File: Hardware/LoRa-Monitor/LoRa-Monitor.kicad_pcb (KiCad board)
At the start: 4 copper layers, 102.6 x 148 mm, 246 parts, among them J1 USB_C_Receptacle_USB2.0_16P, J10 AudioJack3, J11 Screw_Terminal_01x02, J12 Screw_Terminal_01x02, J13 Conn_01x02_Pin, J14 Conn_01x02_Pin, J15 Screw_Terminal_01x03, J2 Micro_SD_Card, J3 Conn_02x03_Odd_Even, J4 Conn_Coaxial, J6 Screw_Terminal_01x02, J7 AudioJack3, J8 AudioJack3, J9 Screw_Terminal_01x04, Q1 MMBT5551L, Q2 MMBT5551L, Q3 MMBT5551L, Q4 MMBT5551L, Q5 MMBT5551L, Q6 MMBT5551L, U1 IRM-05-5, U10 ESP32-S3-WROOM-1, U11 TPS63021DSJR, U12 NXE1S0303MC, U13 NXE1S0303MC, U14 ATM90E32AS-AU-R, U15 E22-900M30S, U16 ADuM1401xRW, U17 ADuM1401xRW, U18 ADuM1401xRW, U2 ACPL-M61L, U3 ACPL-M61L, U4 ACPL-M61L, U5 ACPL-M61L, U6 ACPL-M61L, U7 ACPL-M61L, U8 MAX3485, U9 BQ24072RGT, Y1 16.384MHz

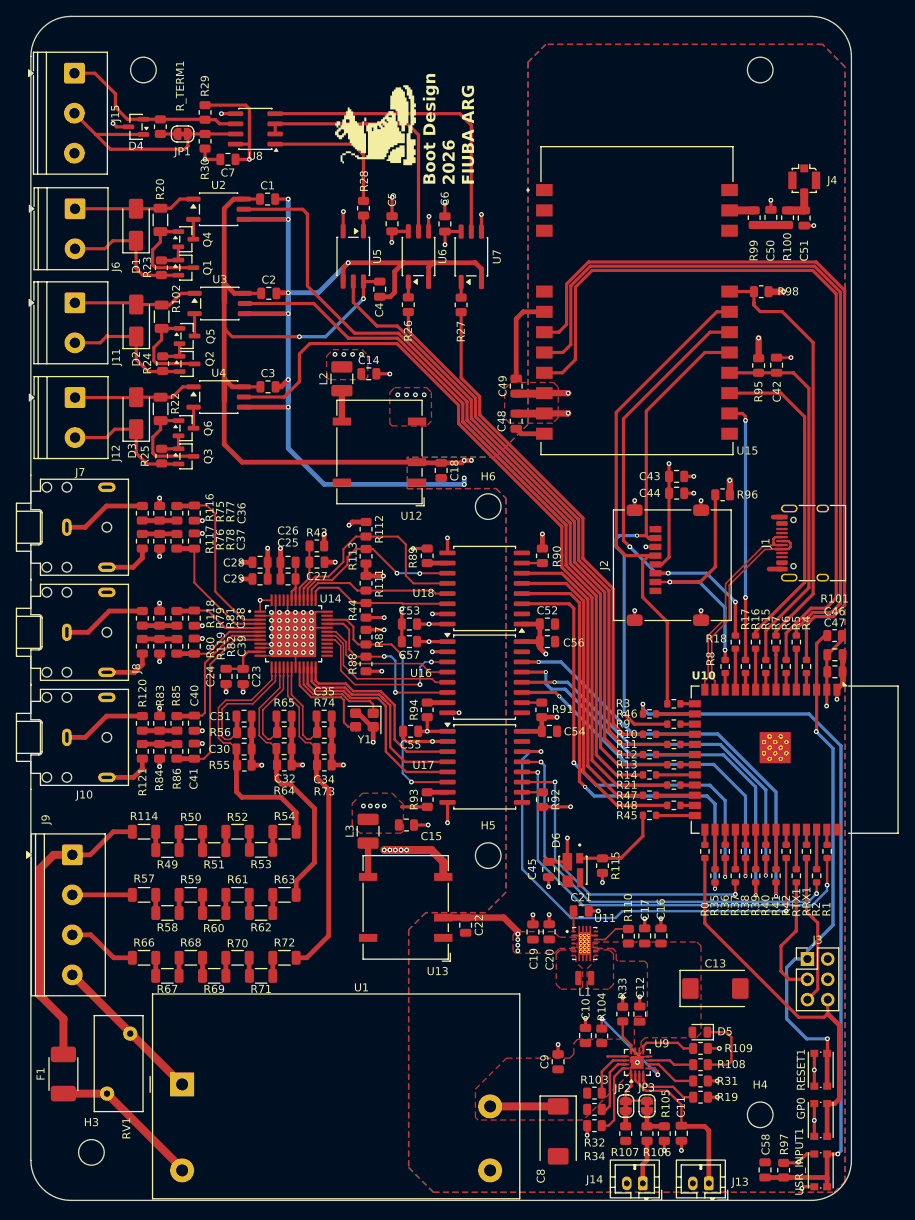
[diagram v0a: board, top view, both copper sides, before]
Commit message: Changed the RS485-TTL translator and its relevent componentes (Power source and optocuplers) for a simpler and easier solution using the ADM2582.
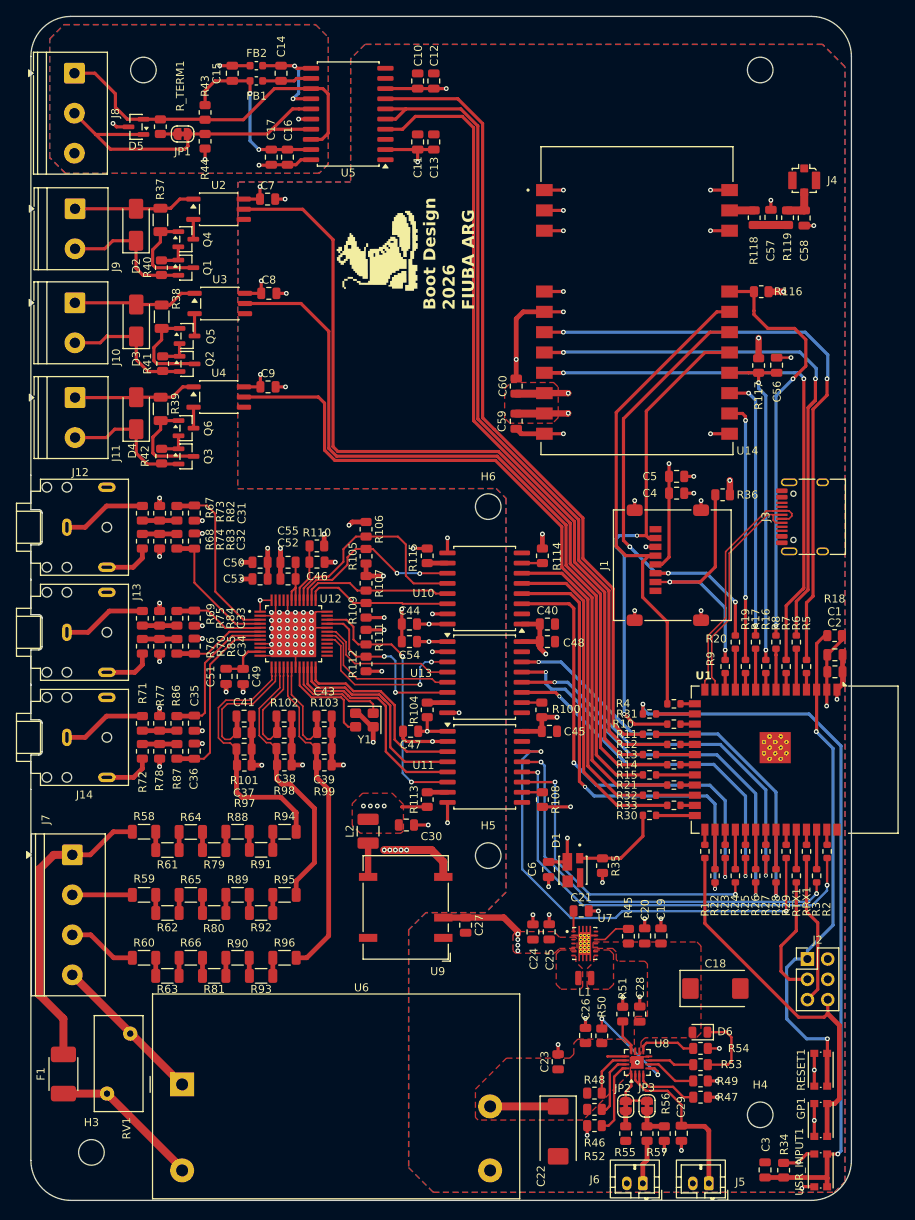
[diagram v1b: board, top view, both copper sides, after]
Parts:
- removed the C14 at (73.7, 66.7)
- removed the C18 at (82.7, 78.8)
- removed the C4 at (75.0, 56.1)
- removed the C6 at (83.2, 47.9)
- removed the C7 at (56.1, 39.9)
- removed the L2 at (70.3, 67.3)
- removed the R26 at (78.6, 58.0)
- removed the R27 at (85.2, 58.1)
- removed the R28 at (73.0, 46.0)
- removed the U12 at (75.0, 75.2)
- removed the U6 at (79.9, 52.0)
- removed the U7 at (86.5, 52.0)
- removed the U8 at (59.5, 36.1)
- added C10: 100nF, Capacitor_SMD:C_0805_2012Metric, F.Cu at (79.8, 30.1)
- added C11: 100nF, Capacitor_SMD:C_0805_2012Metric, F.Cu at (79.8, 37.7)
- added C12: 10uF, Capacitor_SMD:C_0805_2012Metric, F.Cu at (81.8, 30.1)
- added C13: 10nF, Capacitor_SMD:C_0805_2012Metric, F.Cu at (81.8, 37.7)
- added C15: 10uF, Capacitor_SMD:C_0805_2012Metric, F.Cu at (56.6, 29.1)
- added C16: 100nF, Capacitor_SMD:C_0805_2012Metric, F.Cu at (63.5, 39.6)
- added C17: 10nF, Capacitor_SMD:C_0805_2012Metric, F.Cu at (61.5, 39.6)
- added FB1: FerriteBead, Inductor_SMD:L_0603_1608Metric, F.Cu at (59.6, 30.1)
- added FB2: FerriteBead, Inductor_SMD:L_0603_1608Metric, F.Cu at (59.6, 28.2)
- C14: renamed from C5; value 100nF 50V X7R -> 100nF
- U5: value ACPL-M61L -> ADM2582E; footprint DeviceComponents:SO-5_4.39x3.84mm_P1.27mm -> Package_SO:SOIC-20W_7.5x12.8mm_P1.27mm
- moved C14 23.4 mm to (62.7, 29.1)
- moved U5 17.8 mm to (71.1, 34.2), turned to 180 degrees
- moved G*** 15.7 mm to (74.7, 51.3)
- moved J3 3.28 mm to (129.3, 84.5)
- renumbered C46 to C1, C13 to C18, C16 to C19, C47 to C2, C17 to C20, C8 to C22, C9 to C23, C19 to C24, C20 to C25, C10 to C26, C22 to C27, C12 to C28, C11 to C29, C58 to C3, C15 to C30, C36 to C31, C37 to C32, C38 to C33, C39 to C34, C40 to C35, C41 to C36, C30 to C37, C32 to C38, C34 to C39, C44 to C4, C52 to C40, C31 to C41, C33 to C42, C35 to C43, C53 to C44, C54 to C45, C27 to C46, C55 to C47, C56 to C48, C23 to C49, C43 to C5, C28 to C50, C24 to C51, C25 to C52, C29 to C53, C57 to C54, C26 to C55, C42 to C56, C50 to C57, C51 to C58, C48 to C59, C45 to C6, C49 to C60, C1 to C7, C2 to C8, C3 to C9, D6 to D1, D1 to D2, D2 to D3, D3 to D4, D4 to D5, D5 to D6, GP0 to GP1, J2 to J1, J11 to J10, J12 to J11, J7 to J12, J8 to J13, J10 to J14, J3 to J2, J1 to J3, J13 to J5, J14 to J6, J9 to J7, J15 to J8, J6 to J9, L3 to L2, R0 to R1, R9 to R10, R91 to R100, R56 to R101, R65 to R102, R74 to R103, R94 to R104, R113 to R105, R112 to R106, R111 to R107, R92 to R108, R44 to R109, R10 to R11, R43 to R110, R87 to R111, R88 to R112, R93 to R113, R90 to R114, R89 to R115, R98 to R116, R95 to R117, R99 to R118, R100 to R119, R11 to R12, R12 to R13, R13 to R14, R14 to R15, R15 to R16, R16 to R17, R101 to R18, R17 to R19, R1 to R2, R18 to R20, R35 to R22, R36 to R23, R37 to R24, R38 to R25, R39 to R26, R40 to R27, R41 to R28, R42 to R29, R2 to R3, R45 to R30, R46 to R31, R47 to R32, R48 to R33, R97 to R34, R115 to R35, R96 to R36, R20 to R37, R102 to R38, R22 to R39, R3 to R4, R23 to R40, R24 to R41, R25 to R42, R29 to R43, R30 to R44, R110 to R45, R32 to R46, R19 to R47, R103 to R48, R31 to R49, R4 to R5, R104 to R50, R33 to R51, R34 to R52, R108 to R53, R109 to R54, R107 to R55, R105 to R56, R106 to R57, R114 to R58, R57 to R59, R5 to R6, R66 to R60, R49 to R61, R58 to R62, R67 to R63, R50 to R64, R59 to R65, R68 to R66, R116 to R67, R117 to R68, R118 to R69, R6 to R7, R119 to R70, R120 to R71, R121 to R72, R75 to R73, R76 to R74, R79 to R75, R80 to R76, R83 to R77, R84 to R78, R51 to R79, R7 to R8, R60 to R80, R69 to R81, R77 to R82, R78 to R83, R81 to R84, R82 to R85, R85 to R86, R86 to R87, R52 to R88, R61 to R89, R8 to R9, R70 to R90, R53 to R91, R62 to R92, R71 to R93, R54 to R94, R63 to R95, R72 to R96, R55 to R97, R64 to R98, R73 to R99, U10 to U1, U18 to U10, U17 to U11, U14 to U12, U16 to U13, U15 to U14, U1 to U6, U11 to U7, U9 to U8, U13 to U9
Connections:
- C14 pad 1: +3.3V_485 -> Net-(U5-Visoout)
- C14 pad 2: GND_485 -> Net-(C14-Pad2)
- U5 pad 1: Net-(U5-A) -> GND
- U5 pad 3: GND_485 -> GND
- U5 pad 4: GND -> /Energy Meter Interface Module/RXD_485
- U5 pad 5: /Energy Meter Interface Module/RXD_485 -> /Energy Meter Interface Module/EN_485
- U5 pad 6: +3.3V -> /Energy Meter Interface Module/EN_485
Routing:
- net GND: track 195.0 -> 98.2 mm, vias 41 -> 45
- net +3.3V: track 185.5 -> 106.0 mm, vias 21 -> 22
- net Net-(U7-VO): track 38.4 -> 0.00 mm
- net /Energy Meter Interface Module/TXD_485: track 63.6 -> 99.5 mm
- net /Energy Meter Interface Module/EN_485: track 70.7 -> 105.9 mm
- net Net-(U6-VO): track 31.8 -> 0.00 mm
- net /LoRa Module/DIO2_E22: track 97.7 -> 71.1 mm, vias 0 -> 2
- net /Energy Meter Interface Module/RXD_485: track 77.2 -> 101.0 mm
- net /LoRa Module/TXEN_E22: track 93.7 -> 72.7 mm, vias 0 -> 2
- net /Connectors/485_A: track 23.7 -> 44.4 mm
- net /LoRa Module/RXEN_E22: track 95.1 -> 75.8 mm, vias 0 -> 2
- net Net-(U8-RO): track 17.4 -> 0.00 mm
- net /Connectors/485_B: track 29.7 -> 45.3 mm
- net Net-(C14-Pad2): track 0.00 -> 13.0 mm, vias 0 -> 2
- net /Energy Meter Interface Module/PULSE_IN1_3V3: track 102.5 -> 111.1 mm
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- added copper zone on B.Cu, net GND_485
- added copper zone on In2.Cu, net GND_485
- removed copper zone on F.Cu, net +3.3V_485
- removed copper zone on In2.Cu, net +3.3V_485
